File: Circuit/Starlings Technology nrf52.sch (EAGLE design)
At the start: 54 parts, among them IC1 MCP1703CB, J4 USB Micro, J7 CORTEX_DEBUG_SMD, Q2 BSS84, SW1 FSM8JSMASTR, SW2 FSM8JSMASTR, U1 TPS61259YFFR, U2 MCP73831, U3 BC840M, U5 74AHCT2G125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

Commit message: Adjusting traces, submitting to board house.
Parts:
- J1: DIGIKEY A98037-ND -> (none)
- J6: DIGIKEY 277-1860-ND -> (none)
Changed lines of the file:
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@@
 <attribute name="DIGIKEY" value="1914-BC840MCT-ND"/>
 </part>
-<part name="J6" library="SparkFun-Connectors" library_urn="urn:adsk.eagle:library:513" deviceset="CONN_04" device="SCREW" package3d_urn="urn:adsk.eagle:package:38090/1">
-<attribute name="DIGIKEY" value="277-1860-ND"/>
-</part>
+<part name="J6" library="SparkFun-Connectors" library_urn="urn:adsk.eagle:library:513" deviceset="CONN_04" device="SCREW" package3d_urn="urn:adsk.eagle:package:38090/1"/>
 <part name="GND18" library="SparkFun" deviceset="GND" device=""/>
 <part name="J7" library="SparkFun-Connectors" library_urn="urn:adsk.eagle:library:513" deviceset="CORTEX_DEBUG" device="_SMD" package3d_urn="urn:adsk.eagle:package:38289/1">
@@
 <part name="GND11" library="SparkFun-PowerSymbols" deviceset="GND" device=""/>
 <part name="P+7" library="SparkFun-PowerSymbols" deviceset="VCC" device="" value="5V"/>
-<part name="U2" library="SparkFun-IC-Power" deviceset="MCP73831" device="">
+<part name="U2" library="SparkFun-IC-Power" library_urn="urn:adsk.eagle:library:526" deviceset="MCP73831" device="" package3d_urn="urn:adsk.eagle:package:39060/1">
 <attribute name="DIGIKEY" value="MCP73831T-2ACI/OTTR-ND"/>
 </part>
@@
 <part name="P+3" library="SparkFun" deviceset="VCC" device="" value="5V"/>
 <part name="TP5" library="testpad" library_urn="urn:adsk.eagle:library:385" deviceset="TPS" device="B1,27" package3d_urn="urn:adsk.eagle:package:27944/2"/>
-<part name="J1" library="SparkFun-Connectors" library_urn="urn:adsk.eagle:library:513" deviceset="CONN_03" device="SCREW_LOCK" package3d_urn="urn:adsk.eagle:package:38066/1">
-<attribute name="DIGIKEY" value="A98037-ND"/>
-</part>
+<part name="J1" library="SparkFun-Connectors" library_urn="urn:adsk.eagle:library:513" deviceset="CONN_03" device="SCREW_LOCK" package3d_urn="urn:adsk.eagle:package:38066/1"/>
 <part name="GND4" library="SparkFun" deviceset="GND" device=""/>
 <part name="P+10" library="SparkFun-PowerSymbols" deviceset="VCC" device="" value="5V"/>
@@
 <attribute name="VALUE" x="-63.5" y="91.186" size="1.778" layer="96" font="vector" rot="MR180"/>
 <attribute name="NAME" x="-63.5" y="75.692" size="1.778" layer="95" font="vector" rot="MR180"/>
-<attribute name="DIGIKEY" x="-58.42" y="83.82" size="3.4798" layer="96" ratio="10" rot="MR180" display="off"/>
 </instance>
 <instance part="GND18" gate="1" x="137.668" y="81.28" smashed="yes">
@@
 <attribute name="VALUE" x="-63.5" y="109.474" size="1.778" layer="96" font="vector"/>
 <attribute name="NAME" x="-63.5" y="122.428" size="1.778" layer="95" font="vector"/>
-<attribute name="DIGIKEY" x="-60.96" y="116.84" size="3.302" layer="96" display="off"/>
 </instance>
 <instance part="GND4" gate="1" x="-45.72" y="104.14" smashed="yes" rot="MR0">

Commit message: Switching 3.5mm terminal blocks to 2.54mm (0.1") pitch header pins for painless led attachment. Also making buttons perfectly symmetric.
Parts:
- J1: device SparkFun-Connectors:CONN_03SCREW_LOCK -> SparkFun-Connectors:CONN_03LOCK_LONGPADS; DIGIKEY (none) -> S1111EC-03-ND
- J6: device SparkFun-Connectors:CONN_04SCREW -> SparkFun-Connectors:CONN_04LOCK_LONGPADS; DIGIKEY (none) -> S1111EC-04-ND
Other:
- note added: "Revision history: 2022-03-11: Revision 10 - Adding second tactile switch - Adjusting board dimensions to place buttons - Adding rocker on/off switch - Switching LED terminal blocks to .1" headers 2021-06-24: Revision 9 - Moving to nrf52840-DK BSP pins for buttons and leds - Driving LEDs with active LOW - Adding debugging pins for switch and leds 2021-05-24: Revision 8 - Fixed footprint of level s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"
- note removed: "Revision history: 2022-03-11: Revision 10 - Adding second tactile switch - Adjusting board dimensions to place buttons - Adding rocker on/off switch 2021-06-24: Revision 9 - Moving to nrf52840-DK BSP pins for buttons and leds - Driving LEDs with active LOW - Adding debugging pins for switch and leds 2021-05-24: Revision 8 - Fixed footprint of level shifter, XTAL, and connectors - Updated DigiKey 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"
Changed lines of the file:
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@@
 <attribute name="DIGIKEY" value="1914-BC840MCT-ND"/>
 </part>
-<part name="J6" library="SparkFun-Connectors" library_urn="urn:adsk.eagle:library:513" deviceset="CONN_04" device="SCREW" package3d_urn="urn:adsk.eagle:package:38090/1"/>
+<part name="J6" library="SparkFun-Connectors" library_urn="urn:adsk.eagle:library:513" deviceset="CONN_04" device="LOCK_LONGPADS" package3d_urn="urn:adsk.eagle:package:38091/1">
+<attribute name="DIGIKEY" value="S1111EC-04-ND"/>
+</part>
 <part name="GND18" library="SparkFun" deviceset="GND" device=""/>
 <part name="J7" library="SparkFun-Connectors" library_urn="urn:adsk.eagle:library:513" deviceset="CORTEX_DEBUG" device="_SMD" package3d_urn="urn:adsk.eagle:package:38289/1">
@@
 <part name="P+3" library="SparkFun" deviceset="VCC" device="" value="5V"/>
 <part name="TP5" library="testpad" library_urn="urn:adsk.eagle:library:385" deviceset="TPS" device="B1,27" package3d_urn="urn:adsk.eagle:package:27944/2"/>
-<part name="J1" library="SparkFun-Connectors" library_urn="urn:adsk.eagle:library:513" deviceset="CONN_03" device="SCREW_LOCK" package3d_urn="urn:adsk.eagle:package:38066/1"/>
+<part name="J1" library="SparkFun-Connectors" library_urn="urn:adsk.eagle:library:513" deviceset="CONN_03" device="LOCK_LONGPADS" package3d_urn="urn:adsk.eagle:package:38065/1">
+<attribute name="DIGIKEY" value="S1111EC-03-ND"/>
+</part>
 <part name="GND4" library="SparkFun" deviceset="GND" device=""/>
 <part name="P+10" library="SparkFun-PowerSymbols" deviceset="VCC" device="" value="5V"/>
@@
 - Adjusting board dimensions to place buttons
 - Adding rocker on/off switch
+- Switching LED terminal blocks to .1" headers
 2021-06-24: Revision 9
 - Moving to nrf52840-DK BSP pins for buttons and leds
@@
 <attribute name="VALUE" x="-63.5" y="91.186" size="1.778" layer="96" font="vector" rot="MR180"/>
 <attribute name="NAME" x="-63.5" y="75.692" size="1.778" layer="95" font="vector" rot="MR180"/>
+<attribute name="DIGIKEY" x="-58.42" y="83.82" size="1.778" layer="96" rot="MR180" display="off"/>
 </instance>
 <instance part="GND18" gate="1" x="137.668" y="81.28" smashed="yes">
@@
 <attribute name="VALUE" x="-63.5" y="109.474" size="1.778" layer="96" font="vector"/>
 <attribute name="NAME" x="-63.5" y="122.428" size="1.778" layer="95" font="vector"/>
+<attribute name="DIGIKEY" x="-60.96" y="116.84" size="1.778" layer="96" display="off"/>
 </instance>
 <instance part="GND4" gate="1" x="-45.72" y="104.14" smashed="yes" rot="MR0">

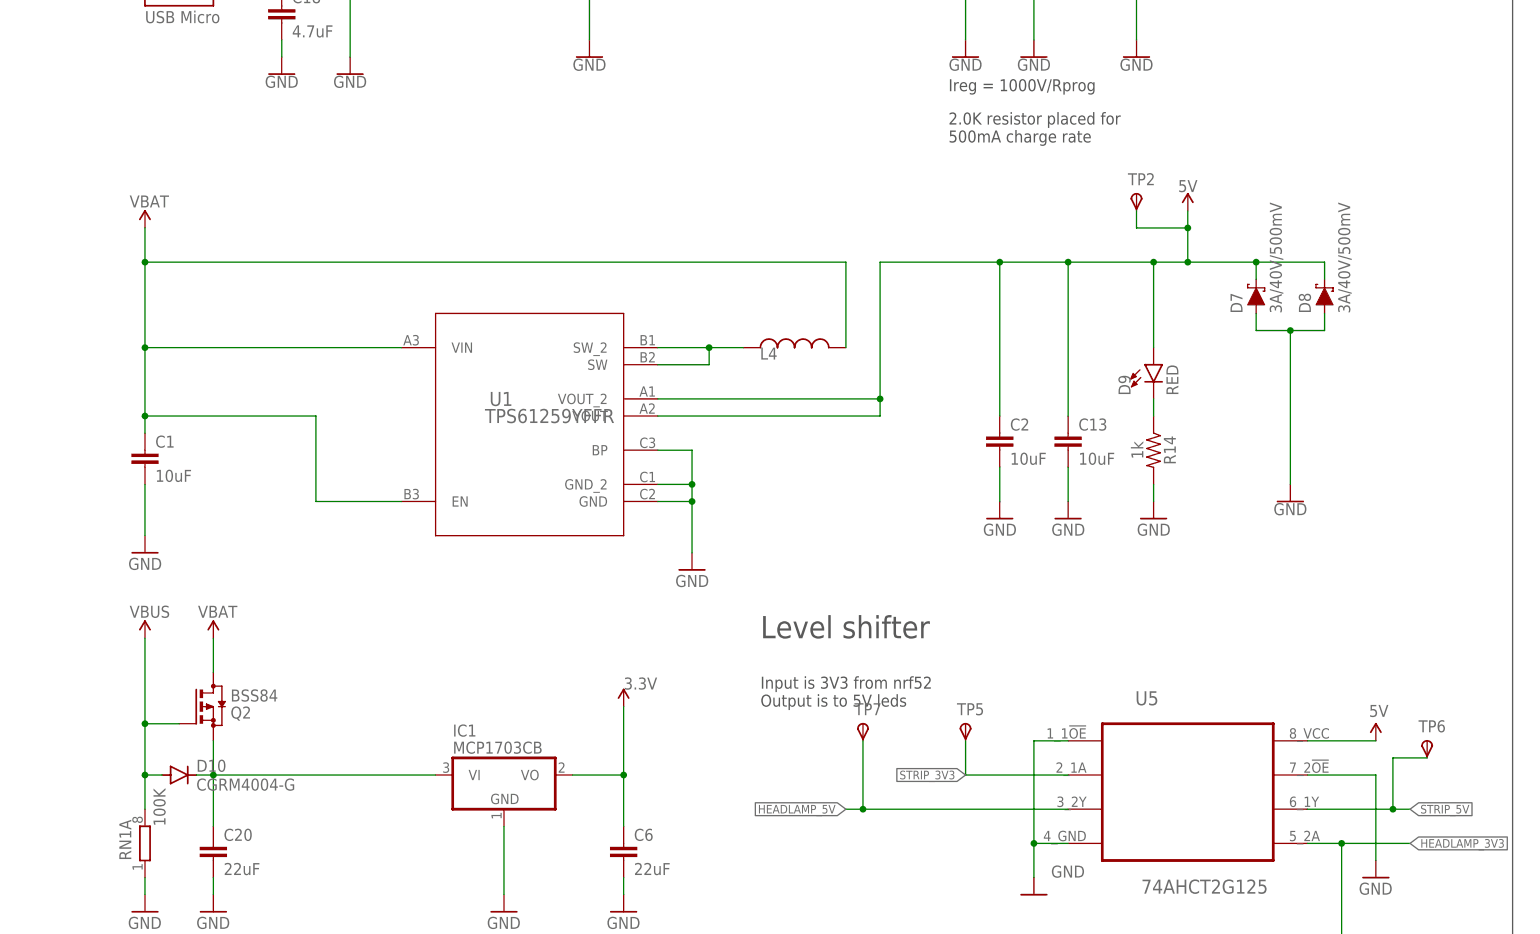
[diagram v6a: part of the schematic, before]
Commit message: Revision 11 of the board, with in stock and bigger boost converter and inductor.
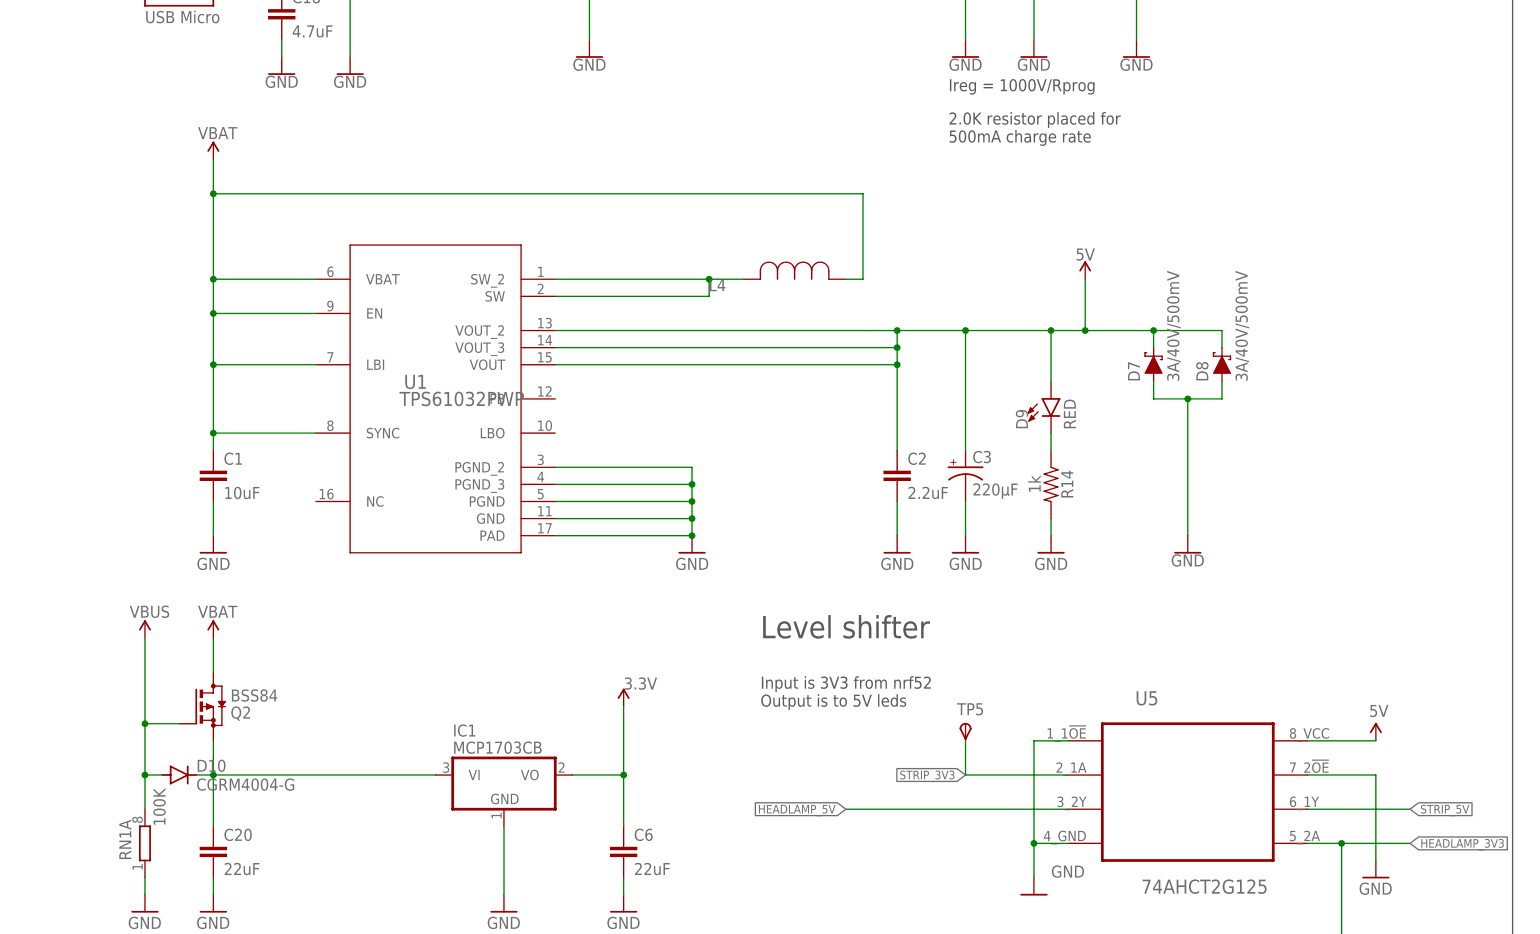
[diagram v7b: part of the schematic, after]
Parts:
- removed C13: 10uF, SparkFun-Capacitors:10UF-0603-6.3V-20%
- removed TP2, TP6, TP7: TPSB1,27, testpad:TPSB1,27
- added C3: 220µF, SparkFun-Capacitors:10UF-POLAR-EIA6032-25V-10%
- C2: value 10uF -> 2.2uF; DIGIKEY 587-1256-1-ND -> 1276-1040-1-ND
- IC1: DIGIKEY AP2138N-3.3TRG1DITR-ND -> AP2138N-3.3TRG1DICT-ND
- L4: device 1277AS-H-1R0M_P2:1277AS-H-1R0M=P2 -> 12mm Inductor:SRR1260-330M; DIGIKEY 490-10590-2-ND -> 308-1937-2-ND
- POWER_IN: DIGIKEY 732-2711-2-ND -> 732-2711-1-ND
- R14: DIGIKEY RMCF0603FG1K00 -> RMCF0603FG1K00CT-ND
- R4, R6: DIGIKEY 311-330HRTR-ND -> 311-330HRCT-ND
- U1: value TPS61259YFFR -> TPS61032PWP; device TPS6125x:TPS61259YFFR -> TPS61031PWPR:TPS61032PWP
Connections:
- net 5V: now also C3.+, U1.VOUT_3; no longer C13.1, TP2.PP
- net GND: now also C3.-, U1.PAD, U1.PGND, U1.PGND_2, U1.PGND_3; no longer C13.2, U1.BP, U1.GND_2
- net HEADLAMP_5V: no longer TP7.PP
- net N$3: now also L4.2; no longer L4.1
- net STRIP_5V: no longer TP6.PP
- net VBAT: now also L4.1, U1.LBI, U1.SYNC, U1.VBAT; no longer L4.2, U1.VIN
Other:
- note added: "Revision history: 2022-04-12: Revision 11 - Switching boost converter and inductor 2022-03-11: Revision 10 - Adding second tactile switch - Adjusting board dimensions to place buttons - Adding rocker on/off switch - Switching LED terminal blocks to .1" headers 2021-06-24: Revision 9 - Moving to nrf52840-DK BSP pins for buttons and leds - Driving LEDs with active LOW - Adding debugging pins for sw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"
- note removed: "Revision history: 2022-03-11: Revision 10 - Adding second tactile switch - Adjusting board dimensions to place buttons - Adding rocker on/off switch - Switching LED terminal blocks to .1" headers 2021-06-24: Revision 9 - Moving to nrf52840-DK BSP pins for buttons and leds - Driving LEDs with active LOW - Adding debugging pins for switch and leds 2021-05-24: Revision 8 - Fixed footprint of level s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"
- moved on the sheet: C1, C2, D7, D8, D9, R14

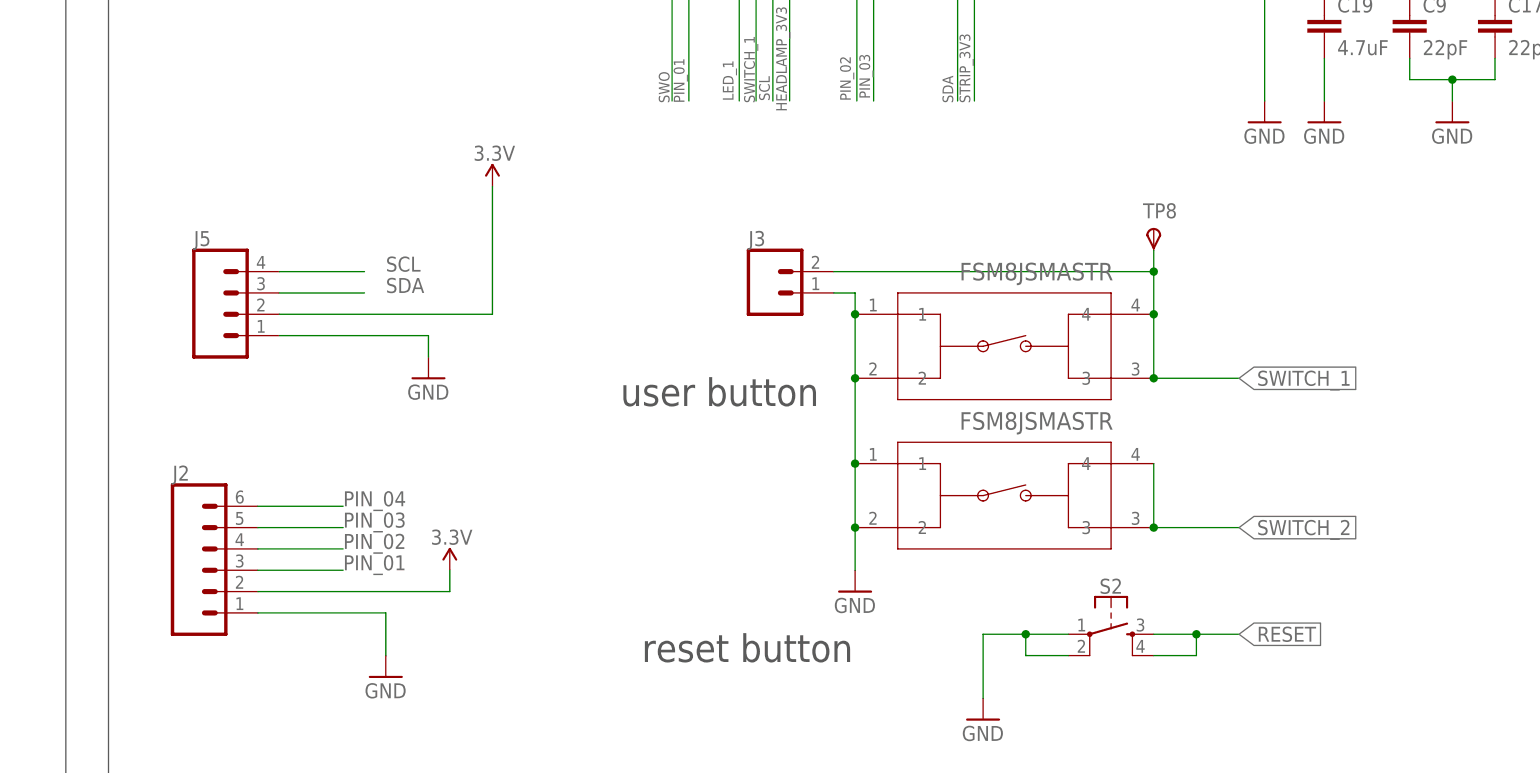
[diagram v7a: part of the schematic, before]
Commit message: Switching to new tactile switches, separating external interfaces for easier reach and to get around enclosure ties.
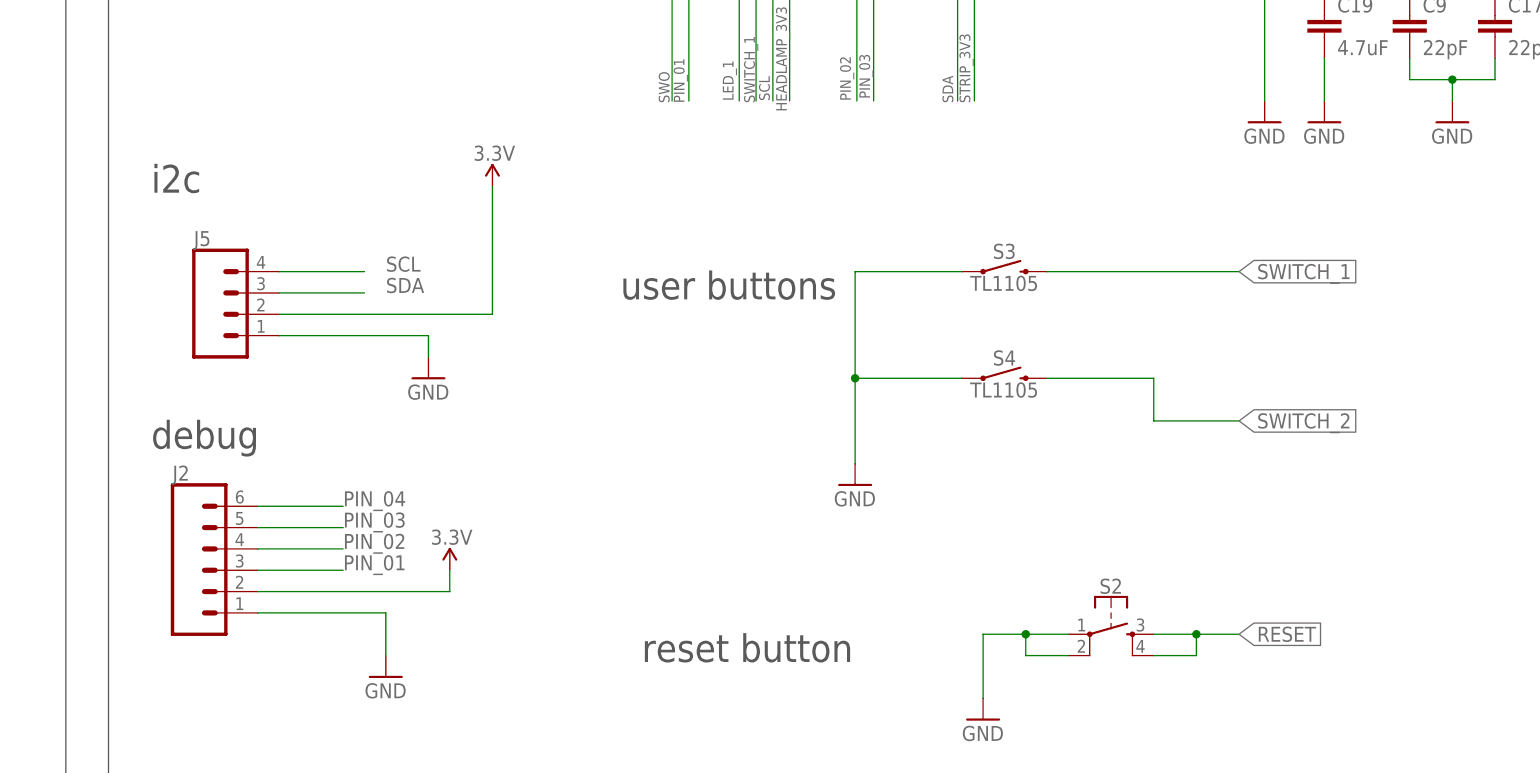
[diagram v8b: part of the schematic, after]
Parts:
- removed J3: (no value), SparkFun-Connectors:CONN_02
- removed SW1, SW2: FSM8JSMASTR, FSM8JSMASTR:FSM8JSMASTR
- removed TP8: TPSB1,27, testpad:TPSB1,27
- added S3, S4: TL1105, SparkFun-Switches:MOMENTARY-SWITCH-SPST-PTH-6.0MM
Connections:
- net GND: now also S3.1, S4.1; no longer J3.1, SW1.1, SW1.2, SW2.1, SW2.2
- net SWITCH_1: now also S3.2; no longer J3.2, SW1.3, SW1.4, TP8.PP
- net SWITCH_2: now also S4.2; no longer SW2.3, SW2.4
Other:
- note added: "debug"
- note added: "i2c"
- note added: "user buttons"
- note removed: "user button"
